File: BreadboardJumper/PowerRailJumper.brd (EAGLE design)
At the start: 10 x 53 mm, 4 parts

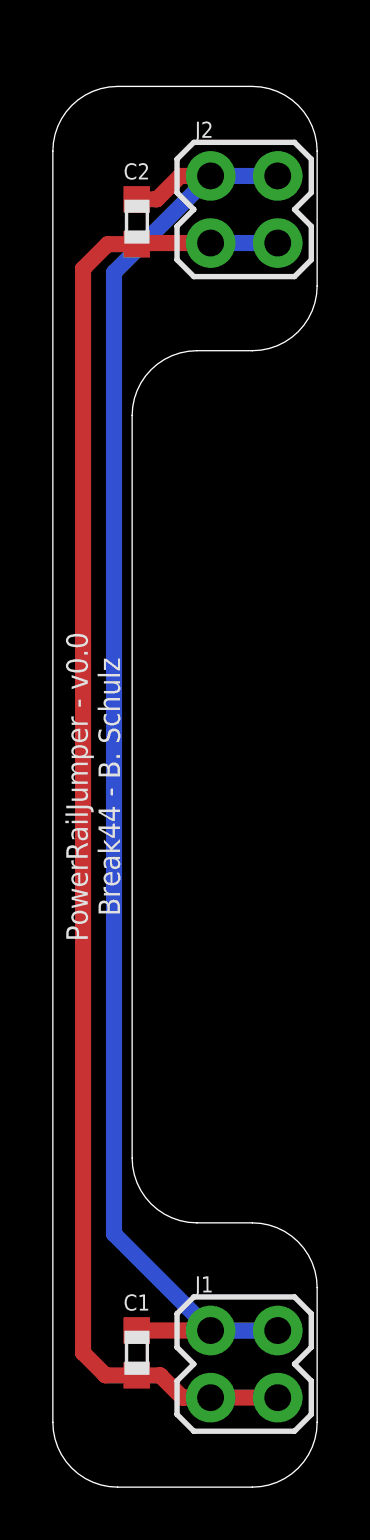
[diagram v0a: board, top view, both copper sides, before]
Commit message: Fix for breadboard jumper
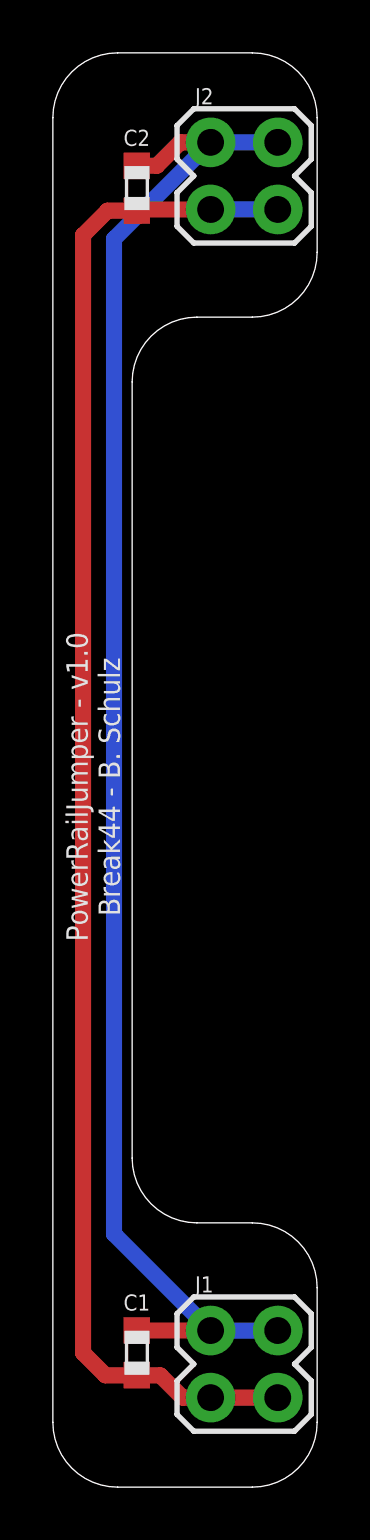
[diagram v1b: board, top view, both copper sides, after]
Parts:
- moved C2 1.27 mm to (3.17, 49.1)
- moved J2 1.27 mm to (8.51, 50.9)
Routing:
- net VCC: track 57.8 -> 59.0 mm
- net GND: track 56.8 -> 58.1 mm
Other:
- board size 10 x 53 mm -> 10 x 54.3 mm
- board text added: "PowerRailJumper - v1.0 Break44 - B. Schulz"
- board text removed: "PowerRailJumper - v0.0 Break44 - B. Schulz"
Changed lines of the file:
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@@
 <board>
 <plain>
-<wire x1="10" y1="45.45" x2="10" y2="50.55" width="0" layer="20"/>
-<wire x1="10" y1="50.55" x2="7.55" y2="53" width="0" layer="20" curve="90"/>
-<wire x1="7.55" y1="53" x2="2.45" y2="53" width="0" layer="20"/>
-<wire x1="2.45" y1="53" x2="0" y2="50.55" width="0" layer="20" curve="90"/>
-<wire x1="0" y1="50.55" x2="0" y2="2.45" width="0" layer="20"/>
+<wire x1="10" y1="46.72" x2="10" y2="51.82" width="0" layer="20"/>
+<wire x1="10" y1="51.82" x2="7.55" y2="54.27" width="0" layer="20" curve="90"/>
+<wire x1="7.55" y1="54.27" x2="2.45" y2="54.27" width="0" layer="20"/>
+<wire x1="2.45" y1="54.27" x2="0" y2="51.82" width="0" layer="20" curve="90"/>
+<wire x1="0" y1="51.82" x2="0" y2="2.45" width="0" layer="20"/>
 <wire x1="0" y1="2.45" x2="2.45" y2="0" width="0" layer="20" curve="90"/>
 <wire x1="2.45" y1="0" x2="7.55" y2="0" width="0" layer="20"/>
@@
 <wire x1="10" y1="7.55" x2="7.55" y2="10" width="0" layer="20" curve="90"/>
 <wire x1="7.55" y1="10" x2="5.45" y2="10" width="0" layer="20"/>
-<wire x1="5.45" y1="43" x2="7.55" y2="43" width="0" layer="20"/>
-<wire x1="7.55" y1="43" x2="10" y2="45.45" width="0" layer="20" curve="90"/>
+<wire x1="5.45" y1="44.27" x2="7.55" y2="44.27" width="0" layer="20"/>
+<wire x1="7.55" y1="44.27" x2="10" y2="46.72" width="0" layer="20" curve="90"/>
 <wire x1="5.45" y1="10" x2="3" y2="12.45" width="0" layer="20" curve="-90"/>
-<wire x1="3" y1="12.45" x2="3" y2="40.55" width="0" layer="20"/>
-<wire x1="3" y1="40.55" x2="5.45" y2="43" width="0" layer="20" curve="-90"/>
-<text x="1.524" y="26.5" size="0.8128" layer="21" font="vector" ratio="15" rot="R90" align="center">PowerRailJumper - v0.0
+<wire x1="3" y1="12.45" x2="3" y2="41.82" width="0" layer="20"/>
+<wire x1="3" y1="41.82" x2="5.45" y2="44.27" width="0" layer="20" curve="-90"/>
+<text x="1.524" y="26.5" size="0.8128" layer="21" font="vector" ratio="15" rot="R90" align="center">PowerRailJumper - v1.0
 Break44 - B. Schulz</text>
 </plain>
@@
 <attribute name="VALUE" x="1.778" y="5.08" size="0.6096" layer="27" font="vector" ratio="15" rot="R270" align="center"/>
 </element>
-<element name="C2" library="bschulz_passives" package="C0603" value="0.1uF" x="3.175" y="47.879" smashed="yes" rot="R270">
-<attribute name="DIGIKEY" value="490-6051-1-ND" x="-13.335" y="32.639" size="1.778" layer="27" rot="R270" display="off"/>
-<attribute name="MF" value="Murata" x="-13.335" y="32.639" size="1.778" layer="27" rot="R270" display="off"/>
-<attribute name="MPN" value="GCM188R71E104KA57D" x="-13.335" y="32.639" size="1.778" layer="27" rot="R270" display="off"/>
-<attribute name="NAME" x="3.175" y="49.784" size="0.6096" layer="25" font="vector" ratio="15" align="center"/>
-<attribute name="VALUE" x="1.778" y="47.879" size="0.6096" layer="27" font="vector" ratio="15" rot="R270" align="center"/>
+<element name="C2" library="bschulz_passives" package="C0603" value="0.1uF" x="3.175" y="49.149" smashed="yes" rot="R270">
+<attribute name="DIGIKEY" value="490-6051-1-ND" x="-13.335" y="33.909" size="1.778" layer="27" rot="R270" display="off"/>
+<attribute name="MF" value="Murata" x="-13.335" y="33.909" size="1.778" layer="27" rot="R270" display="off"/>
+<attribute name="MPN" value="GCM188R71E104KA57D" x="-13.335" y="33.909" size="1.778" layer="27" rot="R270" display="off"/>
+<attribute name="NAME" x="3.175" y="51.054" size="0.6096" layer="25" font="vector" ratio="15" align="center"/>
+<attribute name="VALUE" x="1.778" y="49.149" size="0.6096" layer="27" font="vector" ratio="15" rot="R270" align="center"/>
 </element>
 <element name="J1" library="bschulz" package="2X02" value="" x="8.509" y="5.926" smashed="yes" rot="R270">
@@
 <attribute name="VALUE" x="3.937" y="7.196" size="0.6096" layer="27" font="vector" ratio="20" rot="R270"/>
 </element>
-<element name="J2" library="bschulz" package="2X02" value="" x="8.509" y="49.614" smashed="yes" rot="R270">
-<attribute name="NAME" x="5.377" y="51.054" size="0.6096" layer="25" font="vector" ratio="20"/>
-<attribute name="VALUE" x="3.937" y="50.884" size="0.6096" layer="27" font="vector" ratio="20" rot="R270"/>
+<element name="J2" library="bschulz" package="2X02" value="" x="8.509" y="50.884" smashed="yes" rot="R270">
+<attribute name="NAME" x="5.377" y="52.324" size="0.6096" layer="25" font="vector" ratio="20"/>
+<attribute name="VALUE" x="3.937" y="52.154" size="0.6096" layer="27" font="vector" ratio="20" rot="R270"/>
 </element>
 </elements>
@@
 <contactref element="C1" pad="1"/>
 <contactref element="C2" pad="1"/>
-<wire x1="4.822" y1="49.614" x2="3.937" y2="48.729" width="0.6096" layer="1"/>
-<wire x1="3.175" y1="48.729" x2="3.937" y2="48.729" width="0.6096" layer="1"/>
-<wire x1="4.822" y1="49.614" x2="5.969" y2="49.614" width="0.6096" layer="1"/>
+<wire x1="4.822" y1="50.884" x2="3.937" y2="49.999" width="0.6096" layer="1"/>
+<wire x1="3.175" y1="49.999" x2="3.937" y2="49.999" width="0.6096" layer="1"/>
+<wire x1="4.822" y1="50.884" x2="5.969" y2="50.884" width="0.6096" layer="1"/>
 <wire x1="3.175" y1="5.93" x2="3.179" y2="5.926" width="0.6096" layer="1"/>
 <wire x1="5.969" y1="5.926" x2="3.179" y2="5.926" width="0.6096" layer="1"/>
 <wire x1="5.969" y1="5.926" x2="8.509" y2="5.926" width="0.6096" layer="16"/>
 <wire x1="5.969" y1="5.926" x2="2.3142" y2="9.5808" width="0.6096" layer="16"/>
-<wire x1="2.3142" y1="45.9592" x2="5.969" y2="49.614" width="0.6096" layer="16"/>
-<wire x1="2.3142" y1="9.5808" x2="2.3142" y2="45.9592" width="0.6096" layer="16"/>
-<wire x1="5.969" y1="49.614" x2="8.509" y2="49.614" width="0.6096" layer="16"/>
+<wire x1="2.3142" y1="47.2292" x2="5.969" y2="50.884" width="0.6096" layer="16"/>
+<wire x1="2.3142" y1="9.5808" x2="2.3142" y2="47.2292" width="0.6096" layer="16"/>
+<wire x1="5.969" y1="50.884" x2="8.509" y2="50.884" width="0.6096" layer="16"/>
 </signal>
 <signal name="GND">
@@
 <contactref element="C1" pad="2"/>
 <contactref element="C2" pad="2"/>
-<wire x1="5.969" y1="47.074" x2="3.22" y2="47.074" width="0.6096" layer="1"/>
+<wire x1="5.969" y1="48.344" x2="3.22" y2="48.344" width="0.6096" layer="1"/>
 <wire x1="5.969" y1="3.386" x2="4.908" y2="3.386" width="0.6096" layer="1"/>
 <wire x1="4.908" y1="3.386" x2="4.064" y2="4.23" width="0.6096" layer="1"/>
 <wire x1="4.064" y1="4.23" x2="3.175" y2="4.23" width="0.6096" layer="1"/>
 <wire x1="5.969" y1="3.386" x2="8.509" y2="3.386" width="0.6096" layer="1"/>
-<wire x1="8.509" y1="47.074" x2="5.969" y2="47.074" width="0.6096" layer="16"/>
+<wire x1="8.509" y1="48.344" x2="5.969" y2="48.344" width="0.6096" layer="16"/>
 <wire x1="3.175" y1="4.23" x2="1.993" y2="4.23" width="0.6096" layer="1"/>
 <wire x1="1.993" y1="4.23" x2="1.143" y2="5.08" width="0.6096" layer="1"/>
-<wire x1="1.143" y1="5.08" x2="1.143" y2="46.101" width="0.6096" layer="1"/>
-<wire x1="1.143" y1="46.101" x2="2.071" y2="47.029" width="0.6096" layer="1"/>
-<wire x1="2.071" y1="47.029" x2="3.175" y2="47.029" width="0.6096" layer="1"/>
-<wire x1="3.175" y1="47.029" x2="3.22" y2="47.074" width="0" layer="19" extent="1-1"/>
+<wire x1="1.143" y1="5.08" x2="1.143" y2="47.371" width="0.6096" layer="1"/>
+<wire x1="1.143" y1="47.371" x2="2.071" y2="48.299" width="0.6096" layer="1"/>
+<wire x1="2.071" y1="48.299" x2="3.175" y2="48.299" width="0.6096" layer="1"/>
+<wire x1="3.175" y1="48.299" x2="3.22" y2="48.344" width="0" layer="19" extent="1-1"/>
 </signal>
 </signals>
